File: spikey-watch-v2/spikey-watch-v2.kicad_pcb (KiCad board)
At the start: 2 copper layers, 48 x 33 mm, 56 parts, among them J1 USB_C_Receptacle_USB2.0_16P, J2 Conn_01x02_Pin, Q1 FDN340P, SW3 USER_SW, SW4 USER_SW, SW7 USER_SW, SW8 USER_SW, U1 ESP32-S3-WROOM-1, U2 USBLC6-2SC6, U3 AP2112K-3.3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

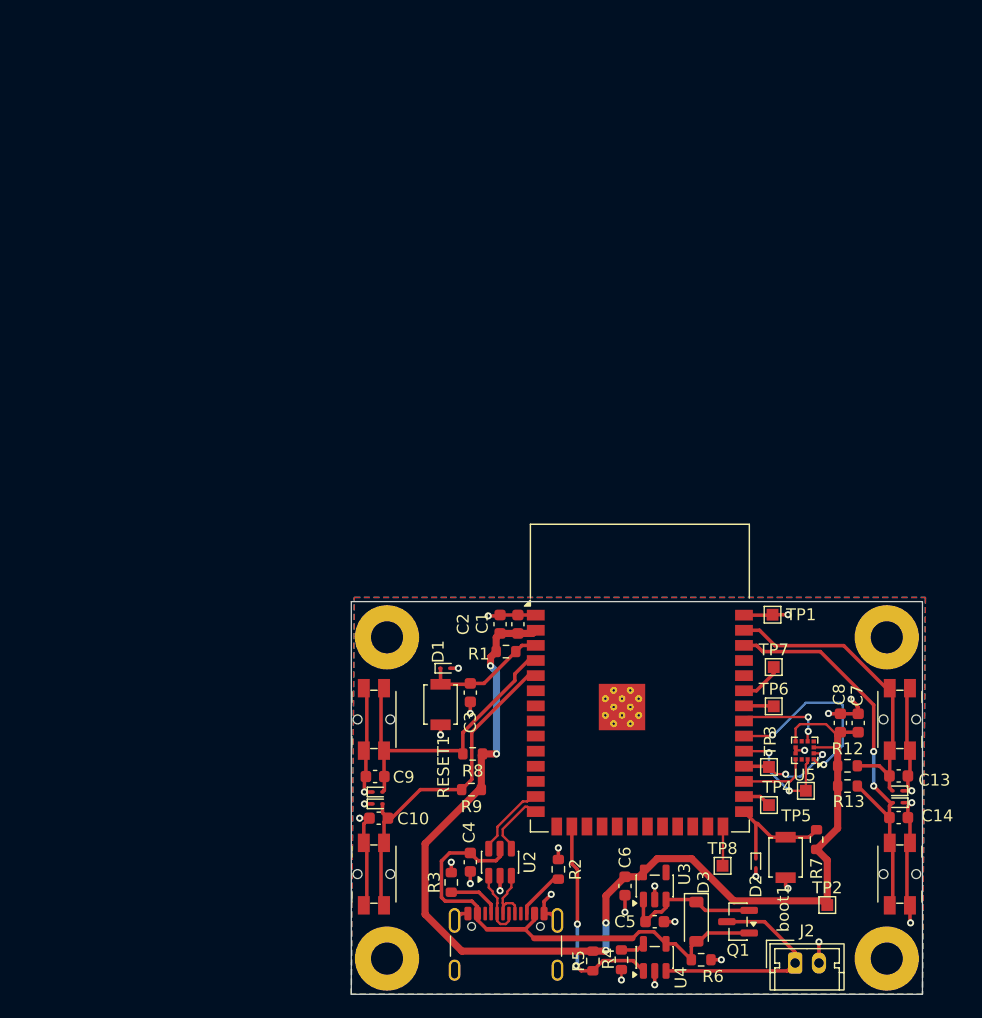
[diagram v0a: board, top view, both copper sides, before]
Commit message: improved routing
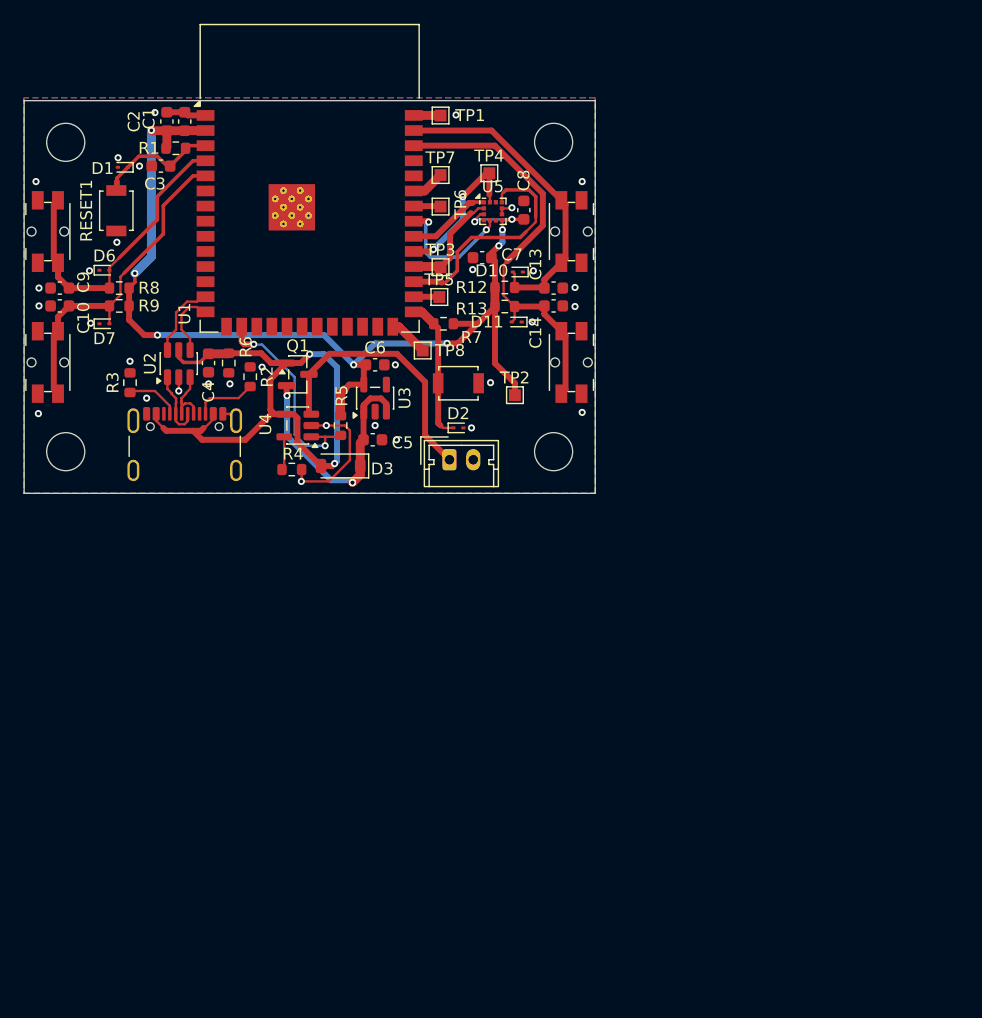
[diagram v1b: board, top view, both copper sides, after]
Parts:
- H1, H2, H3, H4: footprint MountingHole:MountingHole_2.7mm_M2.5_Pad -> MountingHole:MountingHole_3.2mm_M3
- moved H1 97.3 mm to (104.0, 53.0)
- moved R6 64.0 mm to (117.7, 71.5), turned to 90 degrees
- moved Q1 59.0 mm to (123.5, 72.5), turned to 0 degrees
- moved TP4 58.3 mm to (139.6, 55.6)
- moved D10 54.0 mm to (142.0, 63.9)
- moved U4 53.8 mm to (123.5, 76.8), turned to 180 degrees
- moved R7 53.5 mm to (135.8, 68.2), turned to 180 degrees
- moved U5 52.3 mm to (139.9, 58.8), turned to 0 degrees
- moved C14 51.9 mm to (145.0, 66.8)
- moved D11 51.6 mm to (141.9, 68.1)
- moved C3 51.3 mm to (112.0, 55.0), turned to 180 degrees
- moved J2 51.3 mm to (136.2, 79.7)
- moved SW8 51.1 mm to (146.5, 71.5)
- moved SW4 51.0 mm to (102.5, 71.5)
- moved TP5 50.9 mm to (135.4, 66.0)
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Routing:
- net GND: track 74.3 -> 21.2 mm, vias 28 -> 32
- net /CS: track 5.94 -> 19.4 mm
- net +3V3: track 97.8 -> 87.9 mm, vias 4 -> 9
- net VBUS: track 41.7 -> 51.4 mm, vias 0 -> 2
- net /MISO: track 16.2 -> 7.07 mm, vias 2 -> 0
- net /VIN: track 12.2 -> 21.3 mm, vias 0 -> 3
- net /INT1: track 7.59 -> 11.1 mm
- net +BATT: track 18.8 -> 22.3 mm
- net /CLK: track 10.2 -> 12.7 mm
- net Net-(D2-A1): track 10.2 -> 12.0 mm
- net /USER_SW3: track 34.7 -> 35.9 mm, vias 2 -> 0
- net Net-(J1-CC2): track 4.22 -> 5.27 mm
- net /USER_SW1: track 28.8 -> 27.8 mm
- net /RST: track 3.64 -> 2.81 mm
- net Net-(U4-PROG): track 2.06 -> 2.83 mm
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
